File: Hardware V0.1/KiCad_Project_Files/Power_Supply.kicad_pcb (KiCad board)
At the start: 2 copper layers, 100 x 50 mm, 84 parts, among them J2 Conn_01x01, J3 Conn_01x01, J4 Screw_Terminal_01x02, J5 USB_C_Receptacle_USB2.0, J6 Conn_01x04, J7 Conn_01x04, Q1 FDN335N, Q2 FDN335N, SW1 UP, SW2 DW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

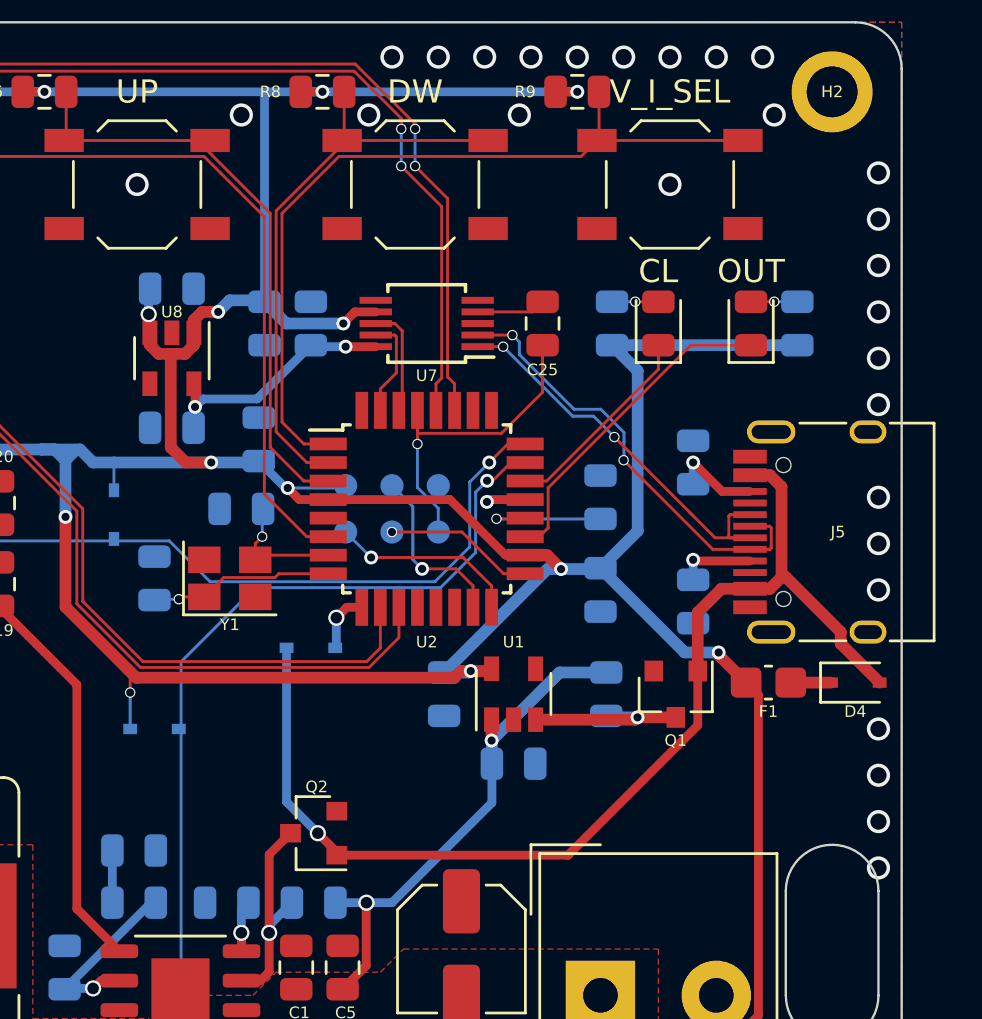
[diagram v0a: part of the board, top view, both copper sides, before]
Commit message: changed MCU to atmega328p for easier arduino dev
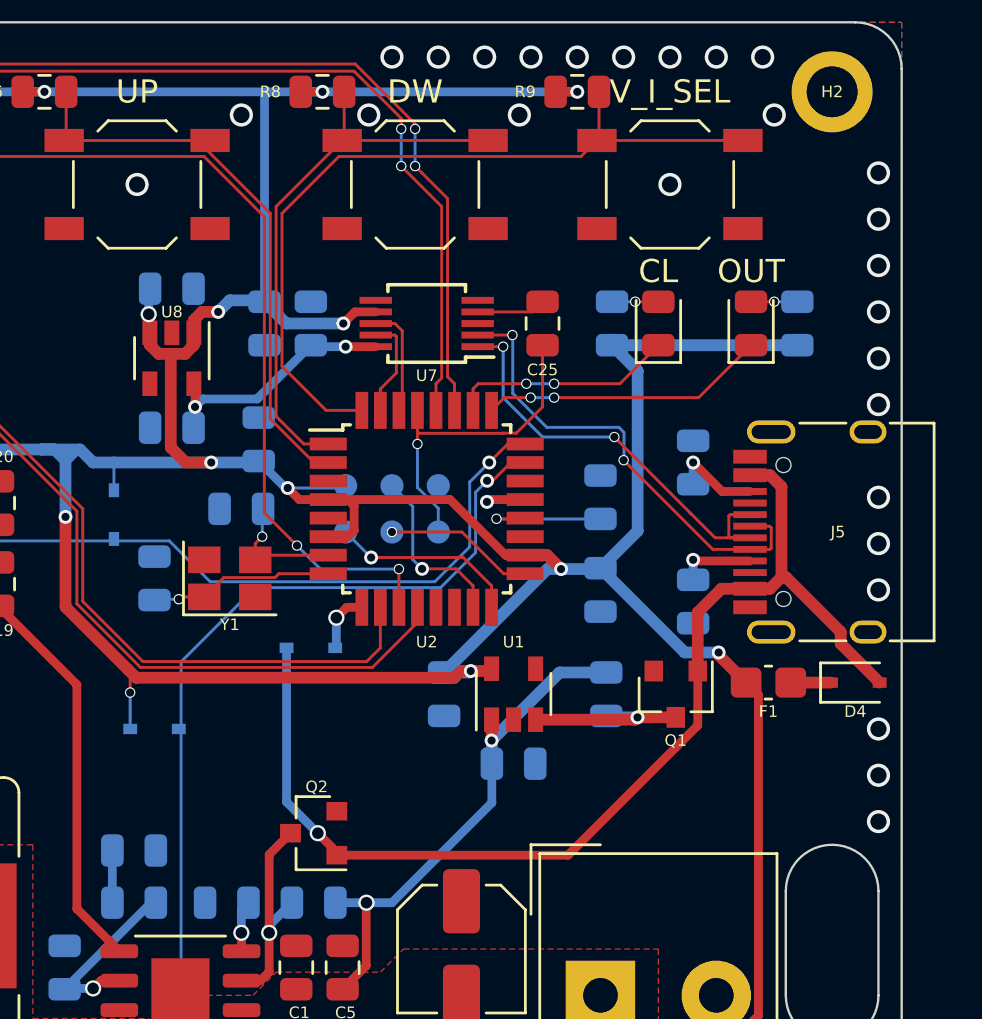
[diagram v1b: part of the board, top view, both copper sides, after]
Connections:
- U2 pad 1: /SW3 -> /SW2
- U2 pad 11: /POT_U~D -> /SW4
- U2 pad 12: (no net) -> /POT_U~D
- U2 pad 19: Net-(D2-Pad1) -> (no net)
- U2 pad 2: /SW2 -> /SW1
- U2 pad 22: Net-(D1-Pad1) -> (no net)
- U2 pad 25: (no net) -> Net-(D2-Pad1)
- U2 pad 26: (no net) -> Net-(D1-Pad1)
- U2 pad 3: /SW1 -> GND
- U2 pad 32: (no net) -> /SW3
- U2 pad 6: /SW4 -> +5V
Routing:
- net /SW4: track 39.6 -> 45.4 mm, vias 0 -> 2
- net +5V: track 292.5 -> 296.1 mm
- net Net-(D2-Pad1): track 14.2 -> 12.4 mm, vias 0 -> 2
- net /D+: track 18.1 -> 19.4 mm
- net /D-: track 19.4 -> 20.5 mm
- net /SW1: track 31.8 -> 30.8 mm
- net Net-(D1-Pad1): track 8.79 -> 9.71 mm, vias 0 -> 2
- net /SW2: track 25.0 -> 24.3 mm
- net /SW3: track 34.7 -> 34.2 mm
- net GND: vias 117 -> 116

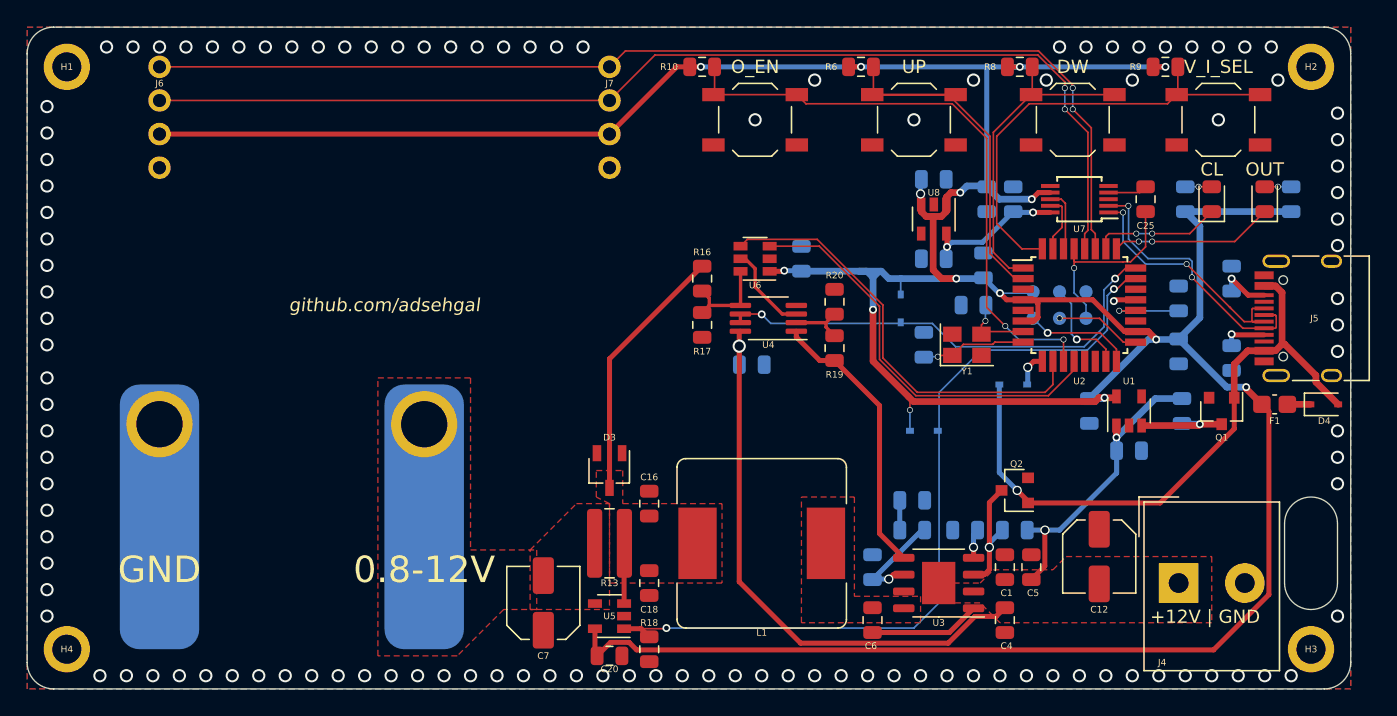
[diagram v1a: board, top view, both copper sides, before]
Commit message: subbed 0.91in with 0.96 OLED
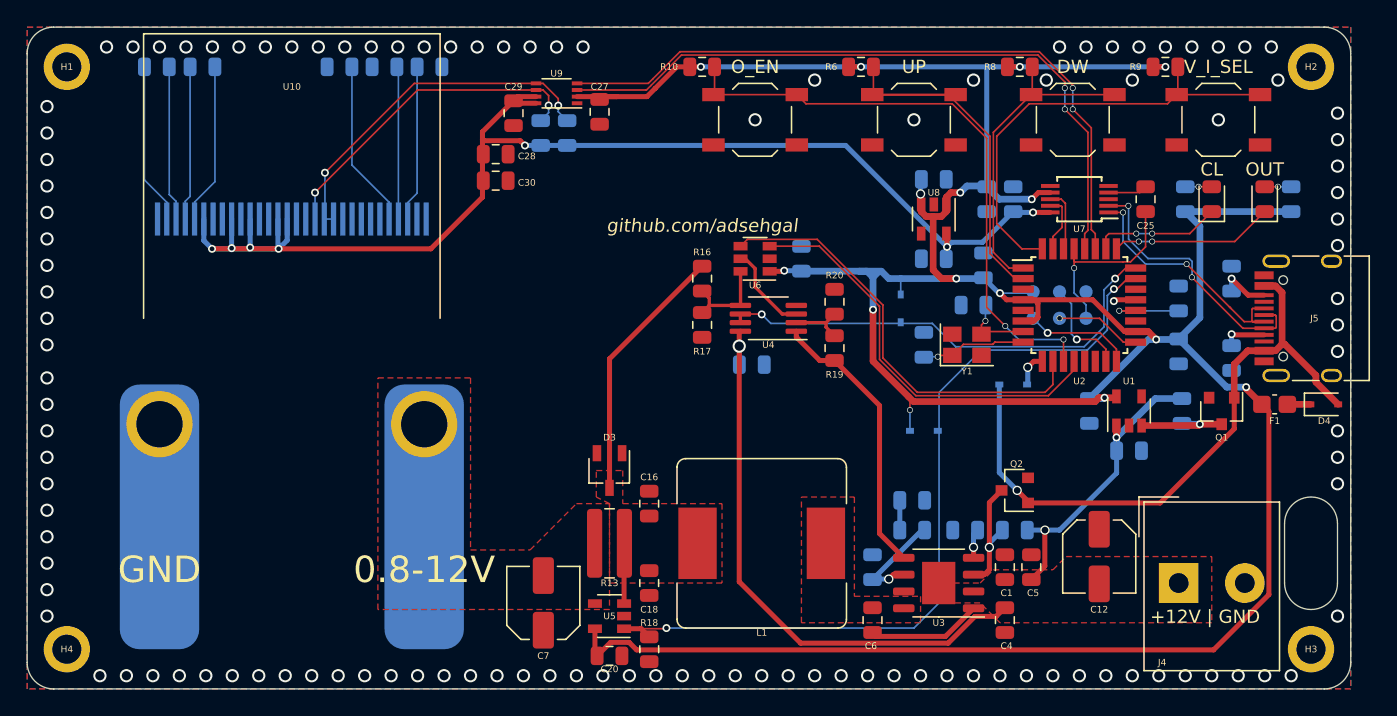
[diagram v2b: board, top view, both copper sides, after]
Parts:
- removed the G*** at (39.5, 29.0)
- removed J6, J7: Conn_01x04, Custom_Vertical_1x_2.54mm_Pin_Header:PinHeader_1x04_P2.54mm_Vertical
- added C27: 100nF, Capacitor_SMD:C_0805_2012Metric, F.Cu at (55.2, 18.4)
- added C28: 100nF, Capacitor_SMD:C_0805_2012Metric, F.Cu at (47.4, 21.6)
- added C29: 1µF, Capacitor_SMD:C_0805_2012Metric, F.Cu at (48.8, 18.5)
- added C30: 1µF, Capacitor_SMD:C_0805_2012Metric, F.Cu at (47.4, 23.6)
- added C31: 1µF, Capacitor_SMD:C_0805_2012Metric, B.Cu at (25.2, 15.0)
- added C32: 4.7µF, Capacitor_SMD:C_0805_2012Metric, B.Cu at (39.0, 15.0)
- added C33: 1µF, Capacitor_SMD:C_0805_2012Metric, B.Cu at (21.8, 15.0)
- added C34: 2.2µF, Capacitor_SMD:C_0805_2012Metric, B.Cu at (42.4, 15.0)
- added G***: LOGO, LOGO, F.Cu at (63.0, 24.0)
- added G***: LOGO, LOGO, B.Cu at (63.0, 24.0)
- added R14: 2.2K, Resistor_SMD:R_0805_2012Metric, B.Cu at (52.8, 20.0)
- added R15: 390K, Resistor_SMD:R_0805_2012Metric, B.Cu at (35.6, 15.0)
- added R5: 2.2K, Resistor_SMD:R_0805_2012Metric, B.Cu at (50.8, 20.0)
- added U10: SSD1306_0.96in, Custom_Displays:SSD1306_0.96in, F.Cu at (32.0, 23.0)
- added U9: PCA9306, Package_SO:VSSOP-8_2.3x2mm_P0.5mm, F.Cu at (52.0, 17.0)
- C21: value C_Small -> 100nF
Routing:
- net +3V3: track 10.9 -> 100.1 mm, vias 2 -> 7
- net /SCL0: track 84.1 -> 52.2 mm
- net +5V: track 296.1 -> 264.8 mm
- net /SDA0: track 83.6 -> 52.6 mm
- net Net-(R14-Pad2): track 0.00 -> 27.1 mm, vias 0 -> 2
- net Net-(R5-Pad2): track 0.00 -> 25.2 mm, vias 0 -> 2
- net Net-(R15-Pad2): track 0.00 -> 12.7 mm
- net Net-(C33-Pad2): track 0.00 -> 12.2 mm
- net Net-(C31-Pad2): track 0.00 -> 12.1 mm
- net Net-(C34-Pad2): track 0.00 -> 11.8 mm
- net Net-(C33-Pad1): track 0.00 -> 11.7 mm
- net Net-(C31-Pad1): track 0.00 -> 11.7 mm
- net Net-(C32-Pad2): track 0.00 -> 11.5 mm

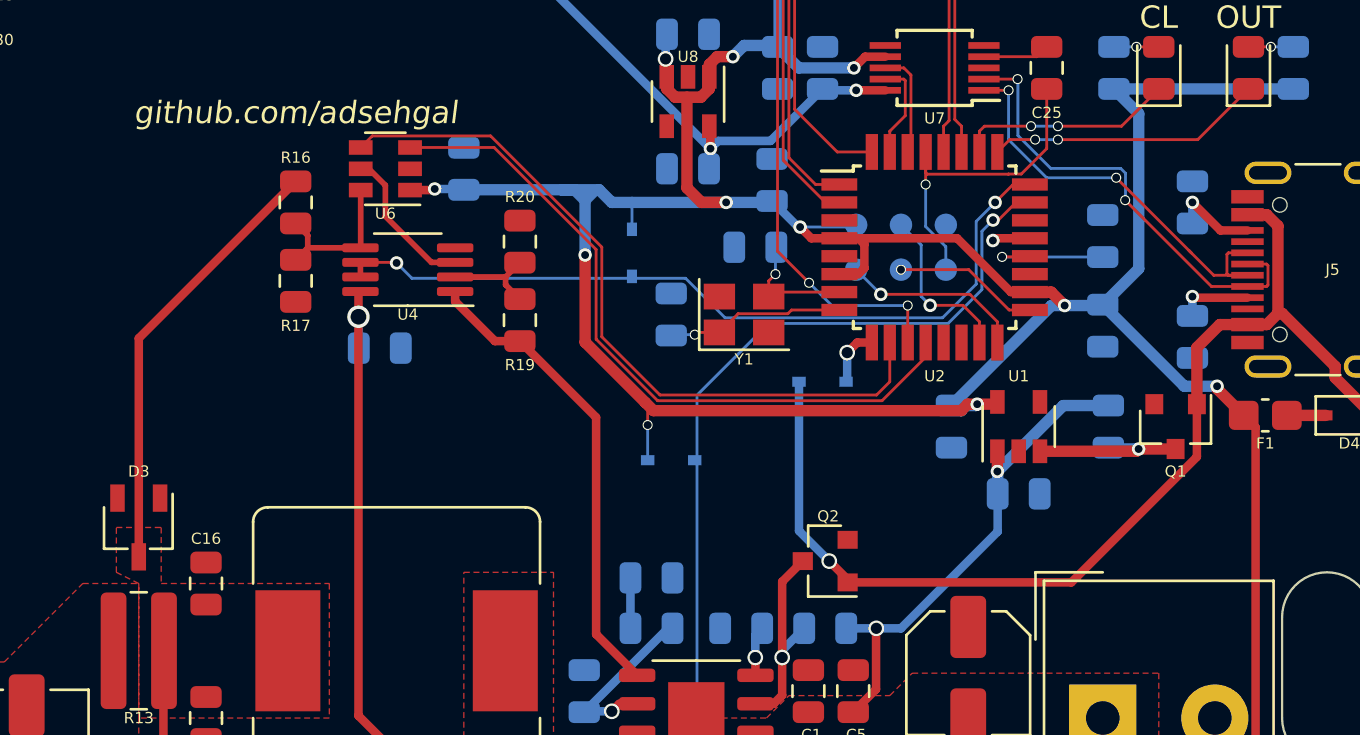
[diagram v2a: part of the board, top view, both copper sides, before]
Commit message: added current limiting resistors on transistors
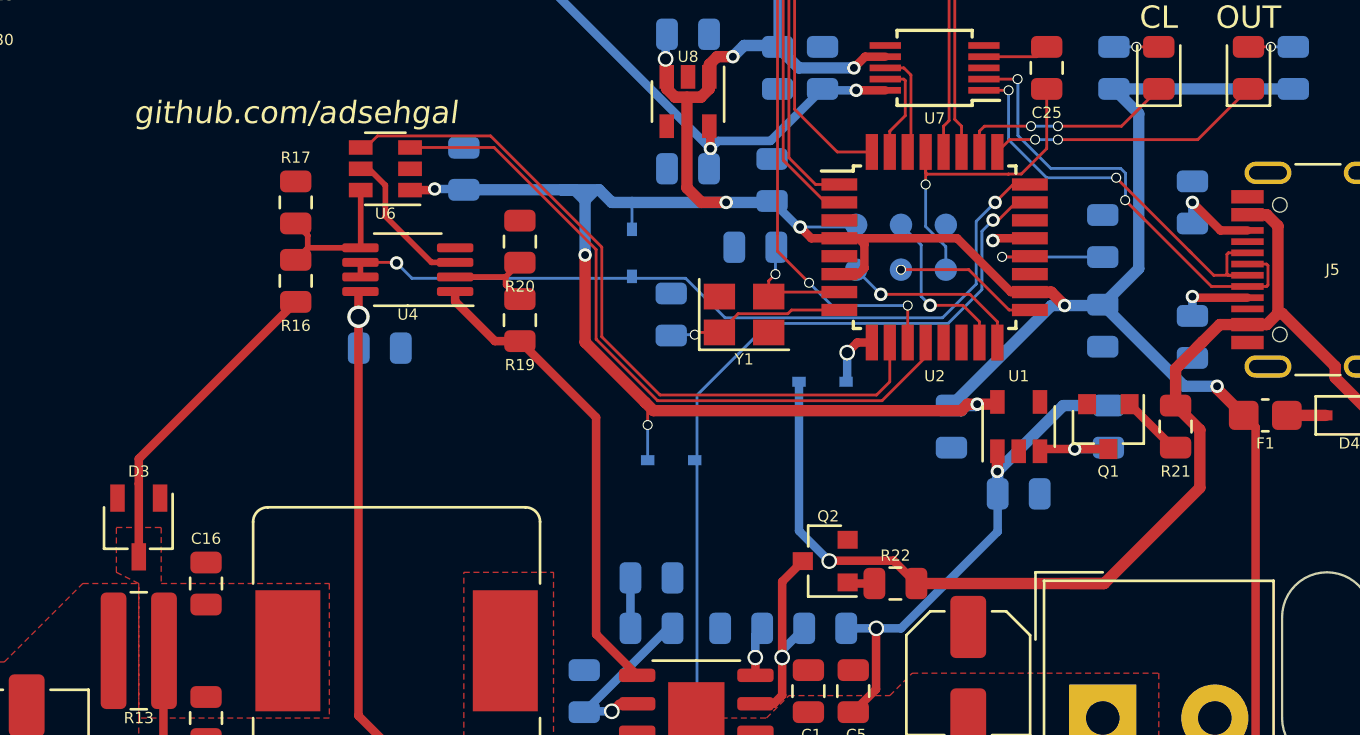
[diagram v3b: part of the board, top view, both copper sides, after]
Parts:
- removed the G*** at (63.0, 24.0) (x2)
- added G***: LOGO, LOGO, F.Cu at (65.0, 24.0)
- added G***: LOGO, LOGO, B.Cu at (65.0, 24.0)
- added R21: 1K, Resistor_SMD:R_0805_2012Metric, F.Cu at (102.2, 41.0)
- added R22: 1K, Resistor_SMD:R_0805_2012Metric, F.Cu at (89.8, 48.0)
- moved R16 3.50 mm to (63.0, 34.5), turned to -90 degrees
- moved R17 3.50 mm to (63.0, 31.0), turned to -90 degrees
- moved Q1 3.00 mm to (99.2, 41.0)
- turned R20 to 90 degrees
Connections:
- Q1 pad 1: /REG_EN -> Net-(Q1-Pad1)
- Q2 pad 1: /REG_EN -> Net-(Q2-Pad1)
- R20 pad 1: GND -> Net-(R19-Pad2)
- R20 pad 2: Net-(R19-Pad2) -> GND
- U10 pad 7: Net-(U10-Pad7) -> (no net)
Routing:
- net Net-(C16-Pad2): track 24.2 -> 18.8 mm
- net /REG_EN: track 48.8 -> 52.5 mm
- net Net-(Q1-Pad1): track 0.00 -> 2.85 mm
- net Net-(Q1-Pad3): track 7.47 -> 4.71 mm
- net Net-(Q2-Pad1): track 0.00 -> 1.34 mm

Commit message: added gerber files, 3-d model and schematic PDF
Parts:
- moved R22 1.00 mm to (89.8, 47.0), turned to 90 degrees
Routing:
- net /REG_EN: track 52.5 -> 49.8 mm, vias 1 -> 3
- net Net-(Q2-Pad1): track 1.34 -> 2.34 mm

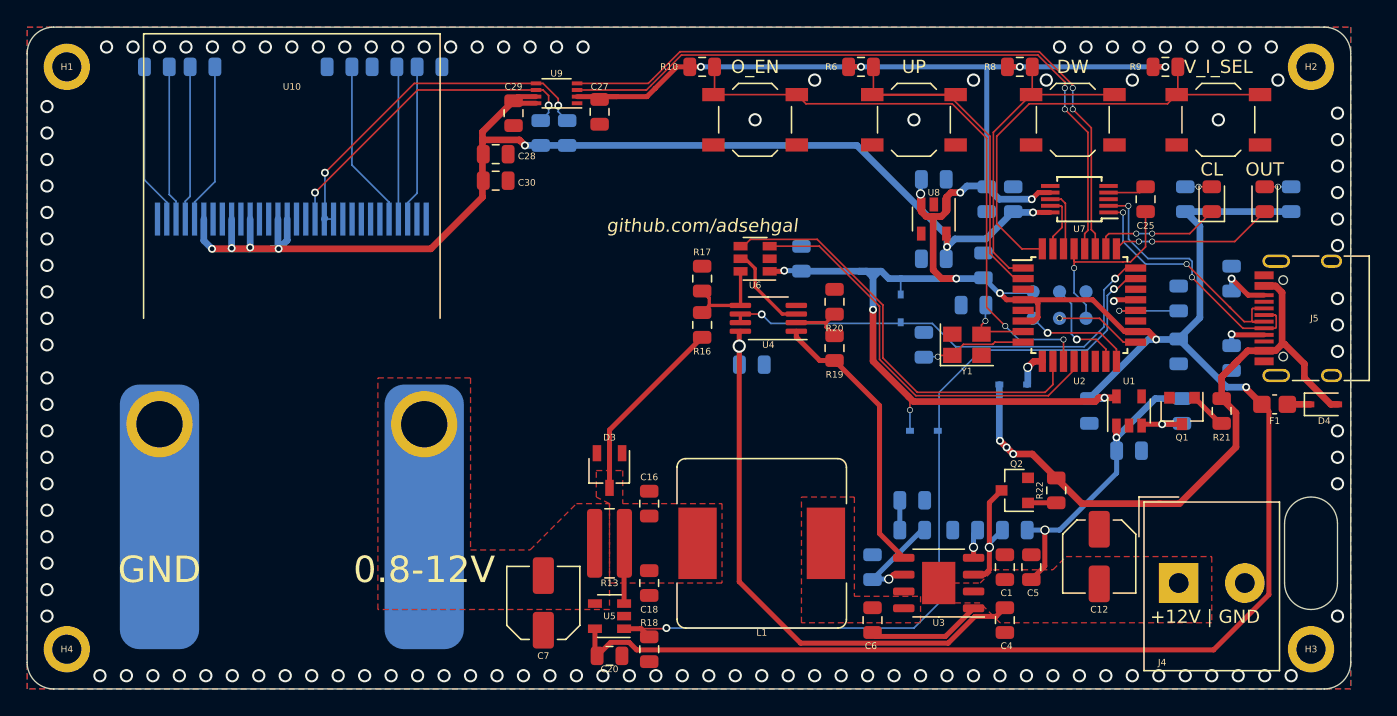
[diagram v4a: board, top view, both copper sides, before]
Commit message: Added Vin measurement
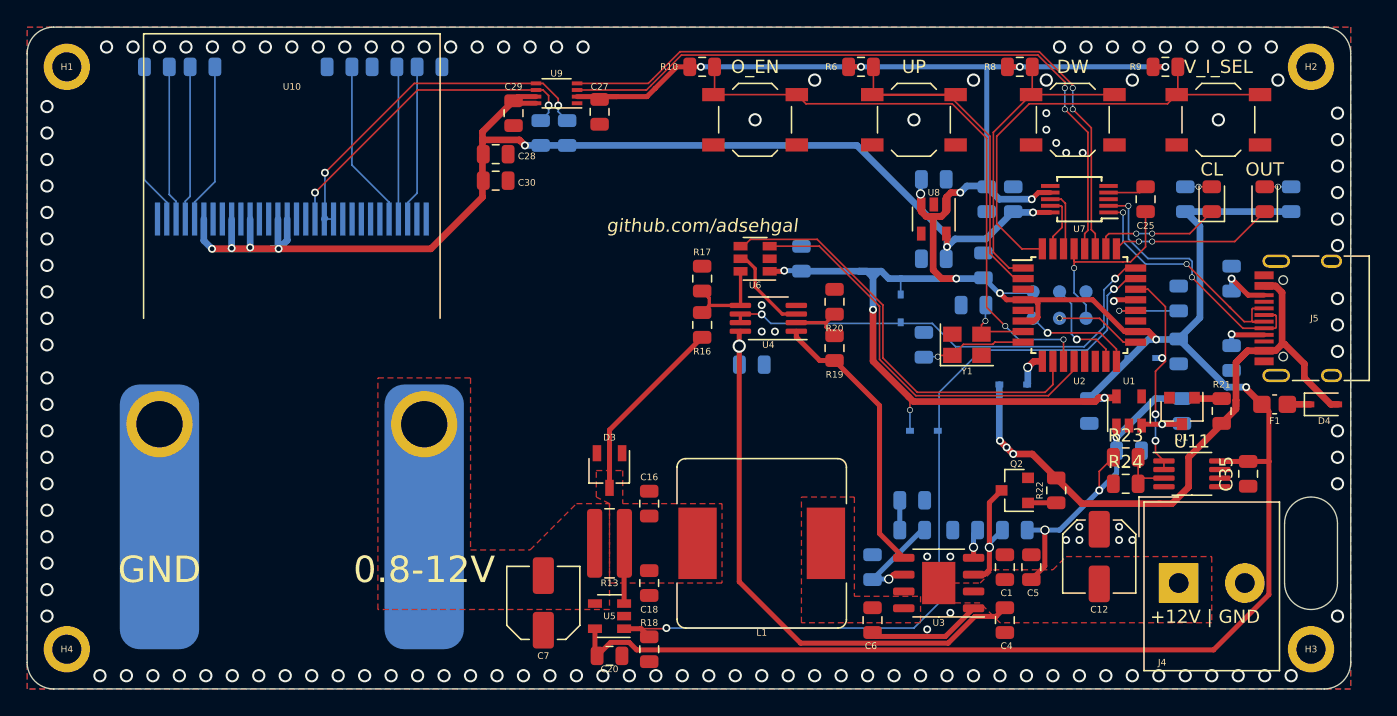
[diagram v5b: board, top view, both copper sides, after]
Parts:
- added C35: 100nF, Capacitor_SMD:C_0805_2012Metric, F.Cu at (104.2, 45.8)
- added D8: CUS10S30, Diode_SMD:D_SOD-323, B.Cu at (96.2, 37.0)
- added R23: 14K, Resistor_SMD:R_0805_2012Metric, F.Cu at (95.0, 44.5)
- added R24: 10K, Resistor_SMD:R_0805_2012Metric, F.Cu at (95.0, 46.5)
- added U11: LM358, Package_SO:MSOP-8_3x3mm_P0.65mm, F.Cu at (100.0, 45.8)
- turned R21 to -90 degrees
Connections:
- U2 pad 22: (no net) -> Net-(D8-Pad2)
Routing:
- net Net-(D8-Pad2): track 0.00 -> 16.4 mm, vias 0 -> 3
- net /Vin: track 0.00 -> 4.13 mm
- net +5V: track 264.8 -> 268.5 mm
- net +VSW: track 65.9 -> 68.9 mm, vias 3 -> 4
- net Net-(Q1-Pad1): track 2.85 -> 2.08 mm
- net Net-(U11-Pad6): track 0.00 -> 0.65 mm
- net GND: vias 116 -> 134
